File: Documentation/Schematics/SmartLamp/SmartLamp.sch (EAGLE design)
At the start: 26 parts, among them IC1 DS3231/SO, J1 POWER_JACKPTH_BREAD, Q1 IRF1404, Q2 IRF1404, Q3 IRF1404, U1 HM-10

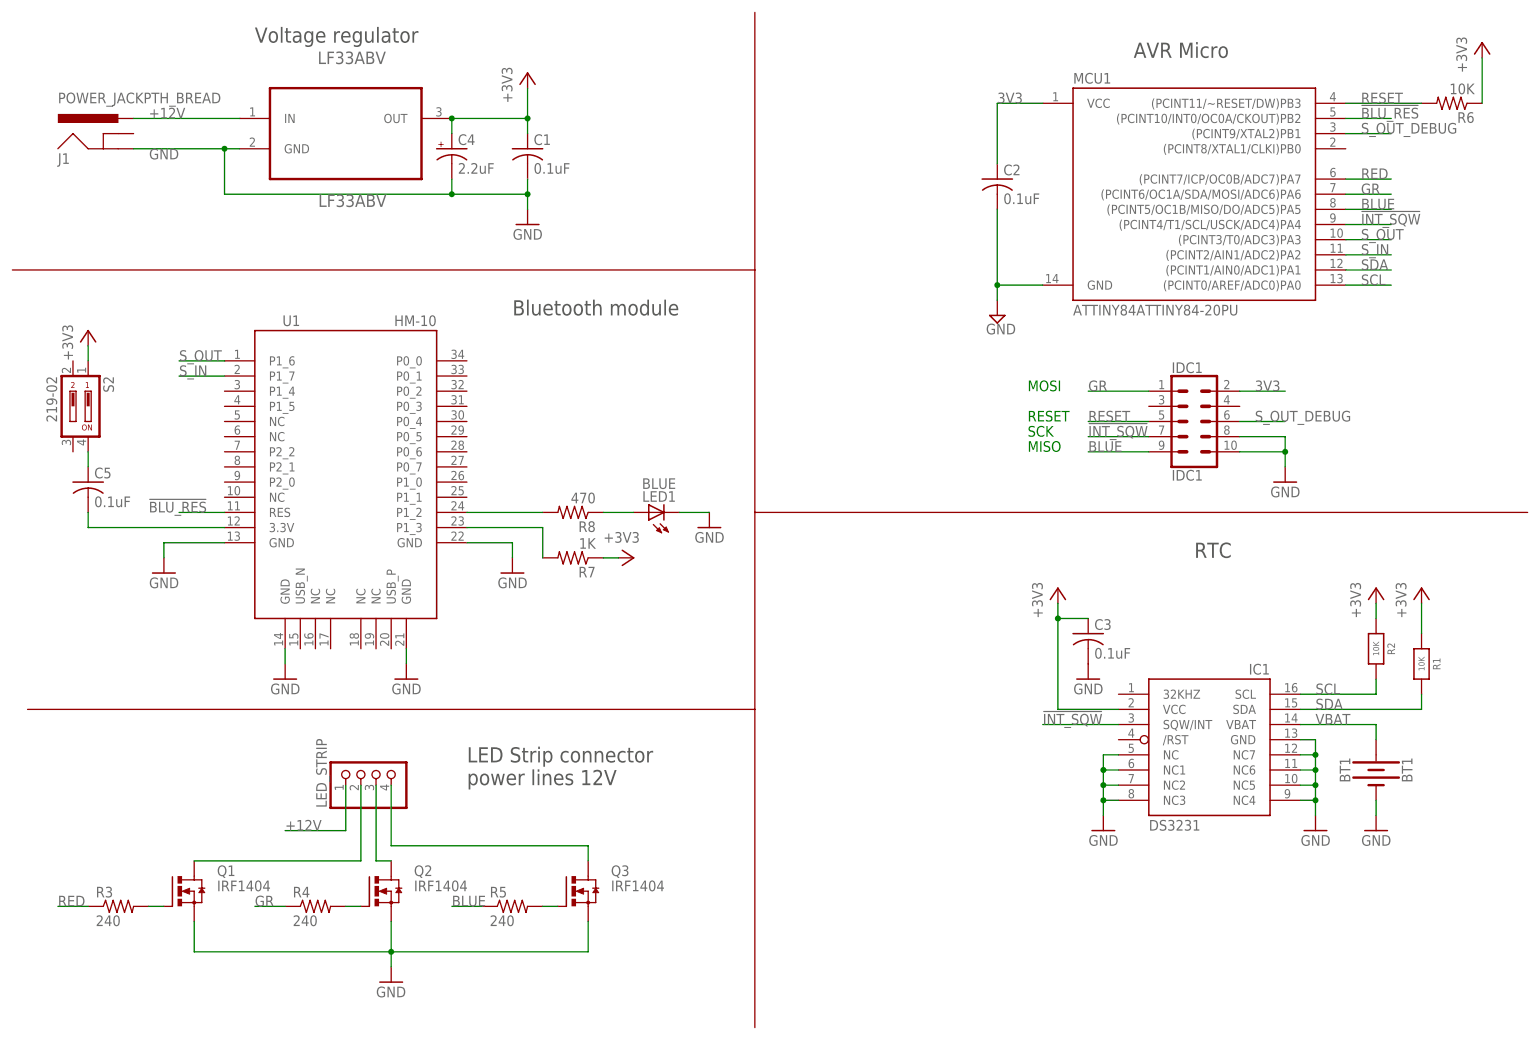
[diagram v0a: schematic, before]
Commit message: Added datasheets of choosen components, first schematic with BOM
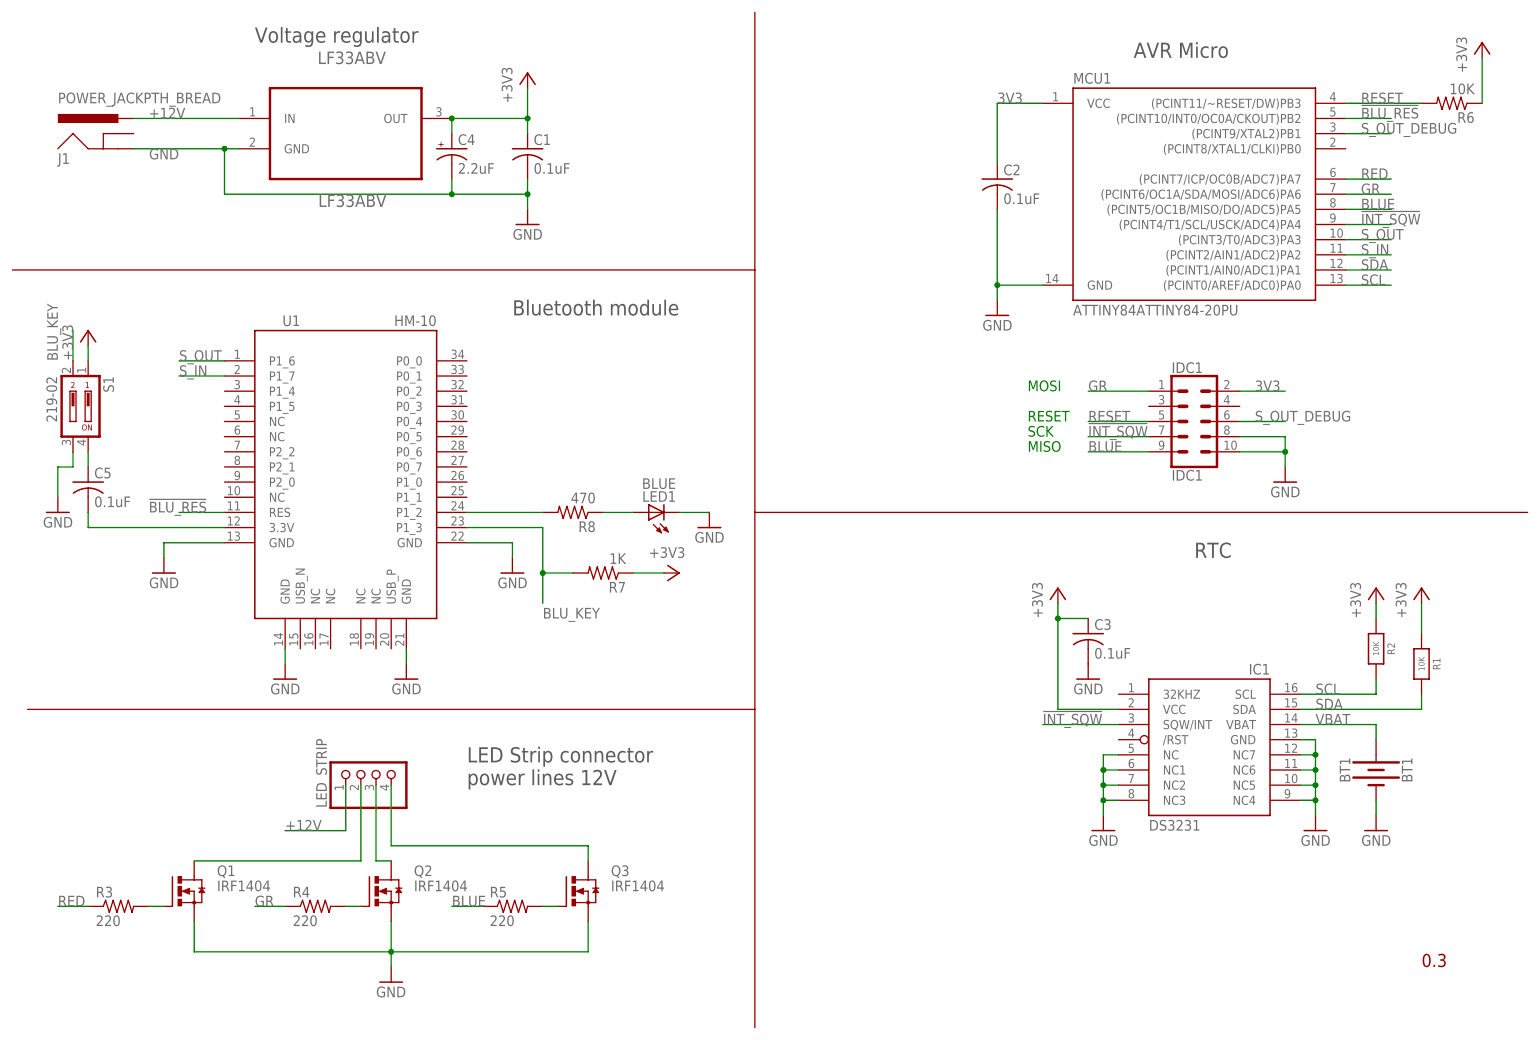
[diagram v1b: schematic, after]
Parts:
- R3, R4, R5: value 240 -> 220
- R6, R8: device rcl:R-US_0207/10 -> rcl:R-US_0309/12
- renumbered S2 to S1
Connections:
- removed net N$12: R7.2, U1.P1_3
- new net BLU_KEY: R7.2, S1.2, U1.P1_3
- net GND: now also S1.3
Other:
- moved on the sheet: R7

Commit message: Added datasheet, replaced 2.2uf cap on schematic with 100uf, to program the Tiny at 3.3v. Added Arduino communication test with HM-10 module.
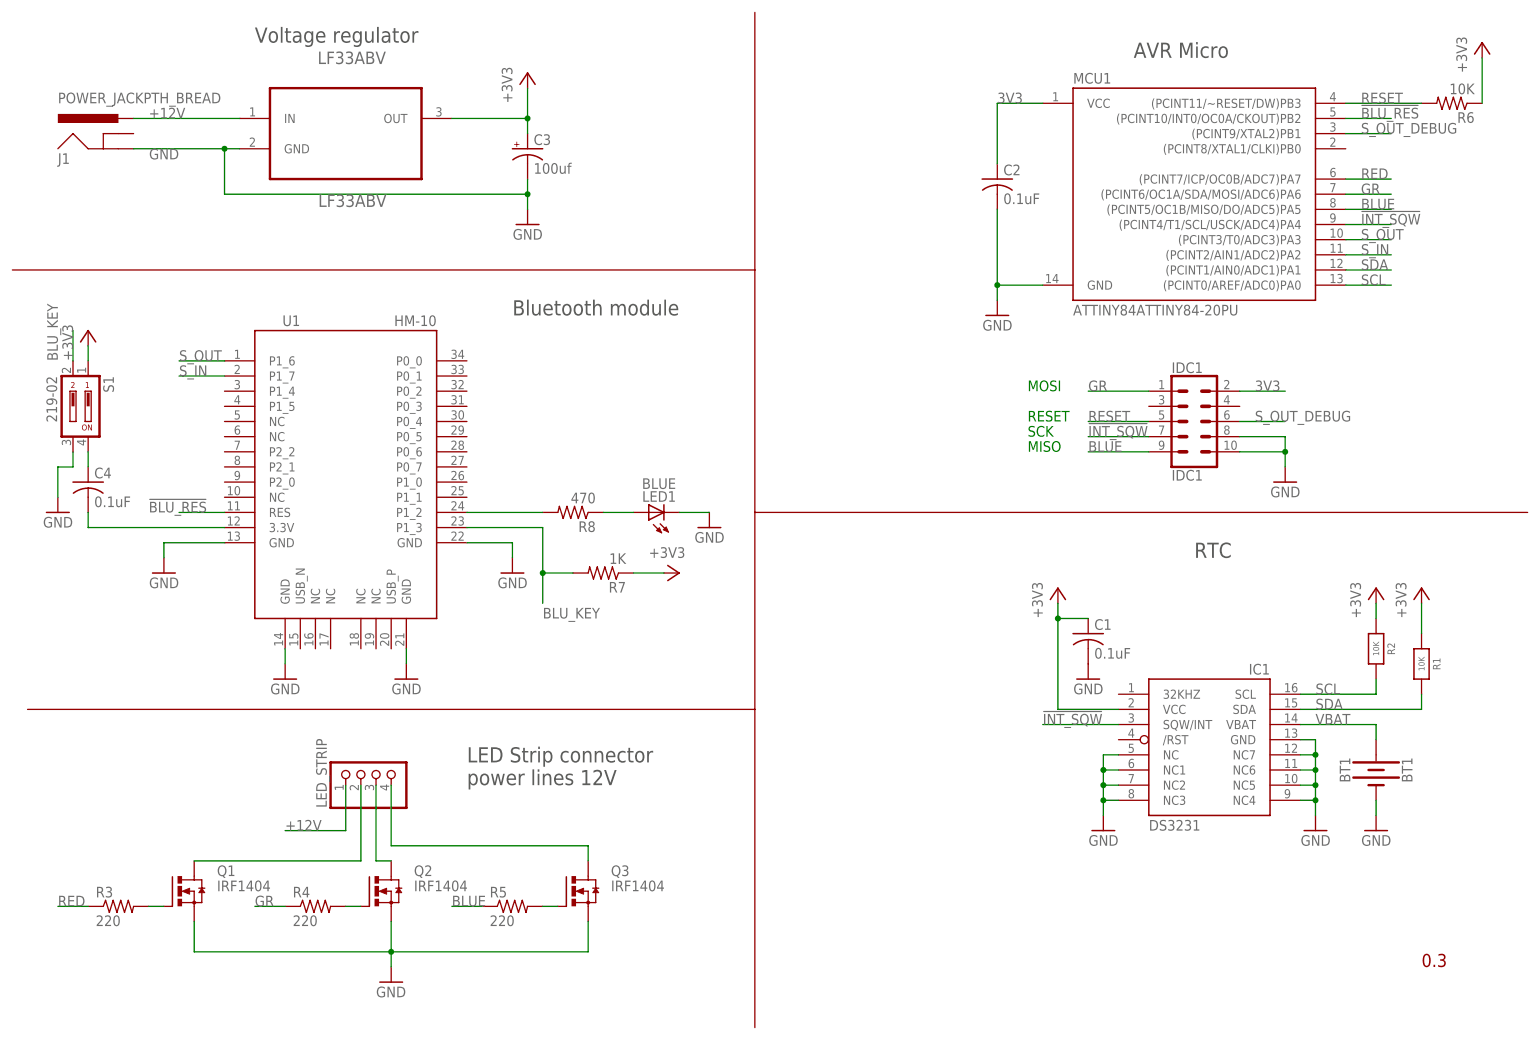
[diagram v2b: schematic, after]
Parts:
- removed C5: 0.1uF, adafruit:C-US025-024X044
- C3: value 0.1uF -> 100uf; device adafruit:C-US025-024X044 -> SparkFun-Capacitors:CAP_POLPTH2
- C4: value 2.2uF -> 0.1uF; device SparkFun-Capacitors:CAP_POLPTH2 -> adafruit:C-US025-024X044
- R1, R2: device microbuilder:RESISTOR0805_NOOUTLINE -> microbuilder:RESISTOR_1206
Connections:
- net +3V3: now also C3.+; no longer C3.1, C4.+
- net GND: now also C3.-; no longer C3.2, C4.-
- net N$1: now also C4.2; no longer C5.2
- net N$2: now also C4.1; no longer C5.1
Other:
- moved on the sheet: C1

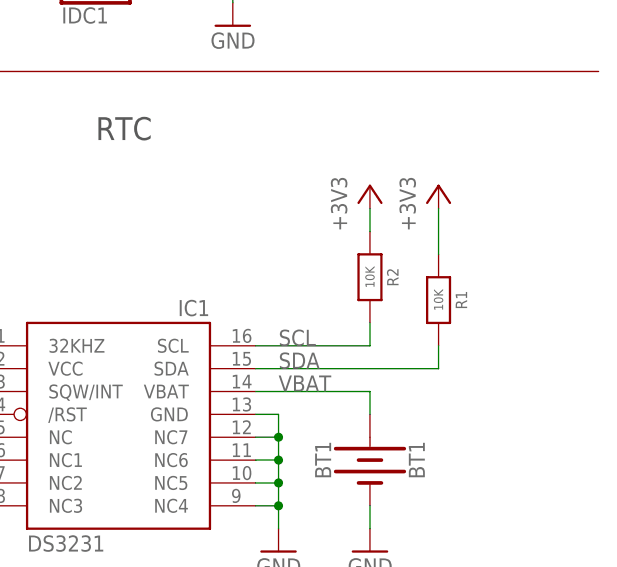
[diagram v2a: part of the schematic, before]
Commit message: Replaced SMD resistors with TH, for this version of the board.
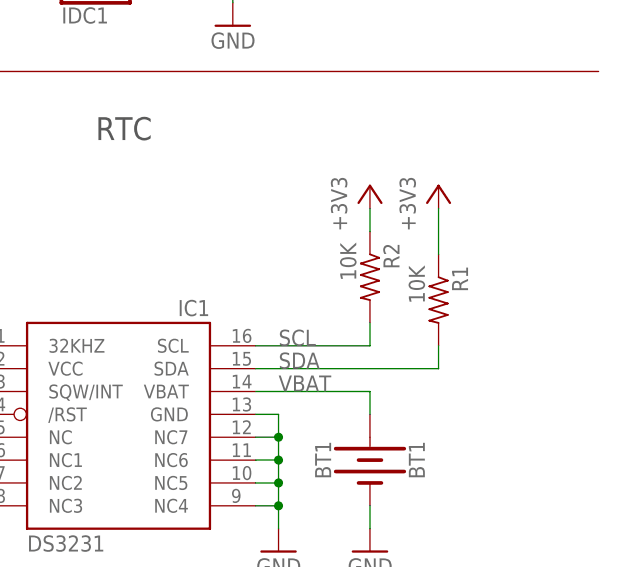
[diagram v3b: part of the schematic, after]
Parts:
- R1, R2: device microbuilder:RESISTOR_1206 -> rcl:R-US_0309/12
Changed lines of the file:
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@@
 <grid distance="0.1" unitdist="inch" unit="inch" style="lines" multiple="1" display="no" altdistance="0.01" altunitdist="inch" altunit="inch"/>
 <layers>
-<layer number="1" name="Top" color="4" fill="1" visible="no" active="no"/>
-<layer number="16" name="Bottom" color="1" fill="1" visible="no" active="no"/>
-<layer number="17" name="Pads" color="2" fill="1" visible="no" active="no"/>
-<layer number="18" name="Vias" color="2" fill="1" visible="no" active="no"/>
-<layer number="19" name="Unrouted" color="6" fill="1" visible="no" active="no"/>
-<layer number="20" name="Dimension" color="15" fill="1" visible="no" active="no"/>
-<layer number="21" name="tPlace" color="7" fill="1" visible="no" active="no"/>
-<layer number="22" name="bPlace" color="7" fill="1" visible="no" active="no"/>
-<layer number="23" name="tOrigins" color="15" fill="1" visible="no" active="no"/>
-<layer number="24" name="bOrigins" color="15" fill="1" visible="no" active="no"/>
-<layer number="25" name="tNames" color="7" fill="1" visible="no" active="no"/>
-<layer number="26" name="bNames" color="7" fill="1" visible="no" active="no"/>
-<layer number="27" name="tValues" color="7" fill="1" visible="no" active="no"/>
-<layer number="28" name="bValues" color="7" fill="1" visible="no" active="no"/>
+<layer number="1" name="Top" color="4" fill="1" visible="yes" active="no"/>
+<layer number="16" name="Bottom" color="1" fill="1" visible="yes" active="no"/>
+<layer number="17" name="Pads" color="2" fill="1" visible="yes" active="no"/>
+<layer number="18" name="Vias" color="2" fill="1" visible="yes" active="no"/>
+<layer number="19" name="Unrouted" color="6" fill="1" visible="yes" active="no"/>
+<layer number="20" name="Dimension" color="15" fill="1" visible="yes" active="no"/>
+<layer number="21" name="tPlace" color="7" fill="1" visible="yes" active="no"/>
+<layer number="22" name="bPlace" color="7" fill="1" visible="yes" active="no"/>
+<layer number="23" name="tOrigins" color="15" fill="1" visible="yes" active="no"/>
+<layer number="24" name="bOrigins" color="15" fill="1" visible="yes" active="no"/>
+<layer number="25" name="tNames" color="7" fill="1" visible="yes" active="no"/>
+<layer number="26" name="bNames" color="7" fill="1" visible="yes" active="no"/>
+<layer number="27" name="tValues" color="7" fill="1" visible="yes" active="no"/>
+<layer number="28" name="bValues" color="7" fill="1" visible="yes" active="no"/>
 <layer number="29" name="tStop" color="7" fill="3" visible="no" active="no"/>
 <layer number="30" name="bStop" color="7" fill="6" visible="no" active="no"/>
@@
 <layer number="35" name="tGlue" color="7" fill="4" visible="no" active="no"/>
 <layer number="36" name="bGlue" color="7" fill="5" visible="no" active="no"/>
-<layer number="37" name="tTest" color="7" fill="1" visible="no" active="no"/>
-<layer number="38" name="bTest" color="7" fill="1" visible="no" active="no"/>
+<layer number="37" name="tTest" color="7" fill="1" visible="yes" active="no"/>
+<layer number="38" name="bTest" color="7" fill="1" visible="yes" active="no"/>
 <layer number="39" name="tKeepout" color="4" fill="11" visible="no" active="no"/>
 <layer number="40" name="bKeepout" color="1" fill="11" visible="no" active="no"/>
@@
 <layer number="44" name="Drills" color="7" fill="1" visible="no" active="no"/>
 <layer number="45" name="Holes" color="7" fill="1" visible="no" active="no"/>
-<layer number="46" name="Milling" color="3" fill="1" visible="no" active="no"/>
-<layer number="47" name="Measures" color="7" fill="1" visible="no" active="no"/>
-<layer number="48" name="Document" color="7" fill="1" visible="no" active="no"/>
-<layer number="49" name="Reference" color="7" fill="1" visible="no" active="no"/>
-<layer number="50" name="dxf" color="7" fill="1" visible="no" active="no"/>
-<layer number="51" name="tDocu" color="7" fill="1" visible="no" active="no"/>
-<layer number="52" name="bDocu" color="7" fill="1" visible="no" active="no"/>
-<layer number="53" name="tGND_GNDA" color="7" fill="9" visible="no" active="no"/>
-<layer number="54" name="bGND_GNDA" color="1" fill="9" visible="no" active="no"/>
-<layer number="56" name="wert" color="7" fill="1" visible="no" active="no"/>
-<layer number="57" name="tCAD" color="7" fill="1" visible="no" active="no"/>
-<layer number="59" name="tCarbon" color="7" fill="1" visible="no" active="no"/>
-<layer number="60" name="bCarbon" color="7" fill="1" visible="no" active="no"/>
+<layer number="46" name="Milling" color="3" fill="1" visible="yes" active="no"/>
+<layer number="47" name="Measures" color="7" fill="1" visible="yes" active="no"/>
+<layer number="48" name="Document" color="7" fill="1" visible="yes" active="no"/>
+<layer number="49" name="Reference" color="7" fill="1" visible="yes" active="no"/>
+<layer number="50" name="dxf" color="7" fill="1" visible="yes" active="no"/>
+<layer number="51" name="tDocu" color="7" fill="1" visible="yes" active="no"/>
+<layer number="52" name="bDocu" color="7" fill="1" visible="yes" active="no"/>
+<layer number="53" name="tGND_GNDA" color="7" fill="9" visible="yes" active="no"/>
+<layer number="54" name="bGND_GNDA" color="1" fill="9" visible="yes" active="no"/>
+<layer number="56" name="wert" color="7" fill="1" visible="yes" active="no"/>
+<layer number="57" name="tCAD" color="7" fill="1" visible="yes" active="no"/>
+<layer number="59" name="tCarbon" color="7" fill="1" visible="yes" active="no"/>
+<layer number="60" name="bCarbon" color="7" fill="1" visible="yes" active="no"/>
 <layer number="90" name="Modules" color="5" fill="1" visible="yes" active="yes"/>
 <layer number="91" name="Nets" color="2" fill="1" visible="yes" active="yes"/>
@@
 </classes>
 <parts>
-<part name="R2" library="microbuilder" deviceset="RESISTOR" device="_1206" value="10K"/>
-<part name="R1" library="microbuilder" deviceset="RESISTOR" device="_1206" value="10K"/>
+<part name="R2" library="rcl" deviceset="R-US_" device="0309/12" value="10K"/>
+<part name="R1" library="rcl" deviceset="R-US_" device="0309/12" value="10K"/>
 <part name="IC1" library="adafruit" deviceset="DS3231" device="/SO"/>
 <part name="GND1" library="supply1" deviceset="GND" device=""/>
